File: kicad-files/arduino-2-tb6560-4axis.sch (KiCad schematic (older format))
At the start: 11 parts, among them J1 DB25_Female_MountingHoles, J2 Conn_01x03_Male, J3 Conn_01x02_Male, J4 Conn_01x02_Male, J5 Conn_01x03_Male, J6 Conn_01x02_Male, J7 Conn_01x03_Male, Q1 2N3904

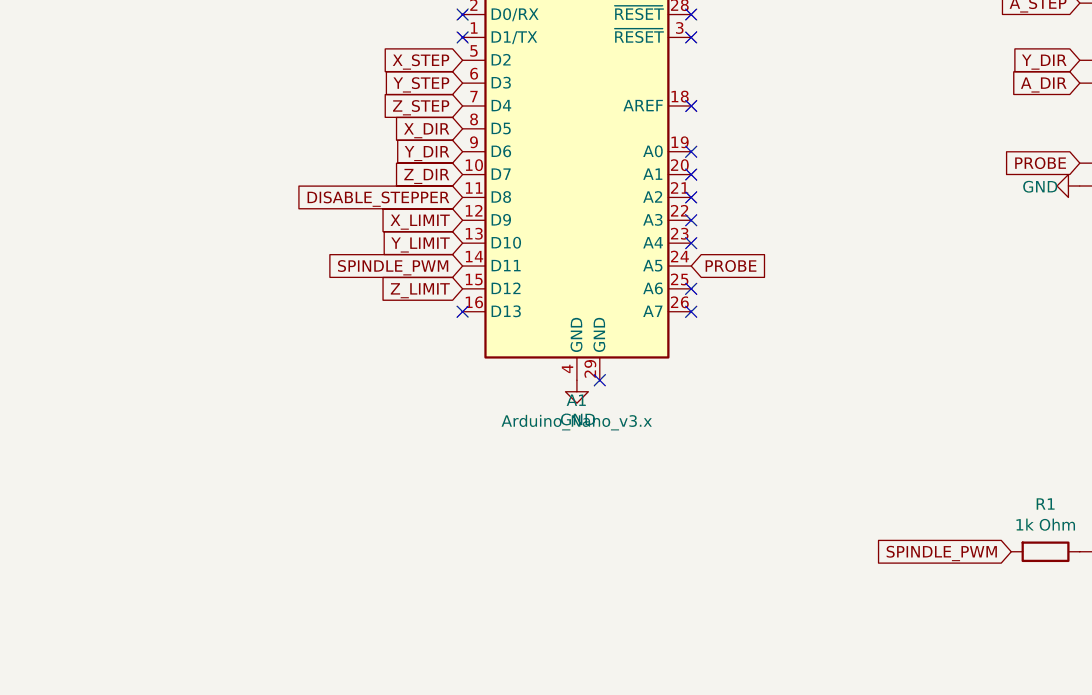
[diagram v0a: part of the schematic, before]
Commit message: added push buttons and jumper header for feed hold and cycle start/resume.
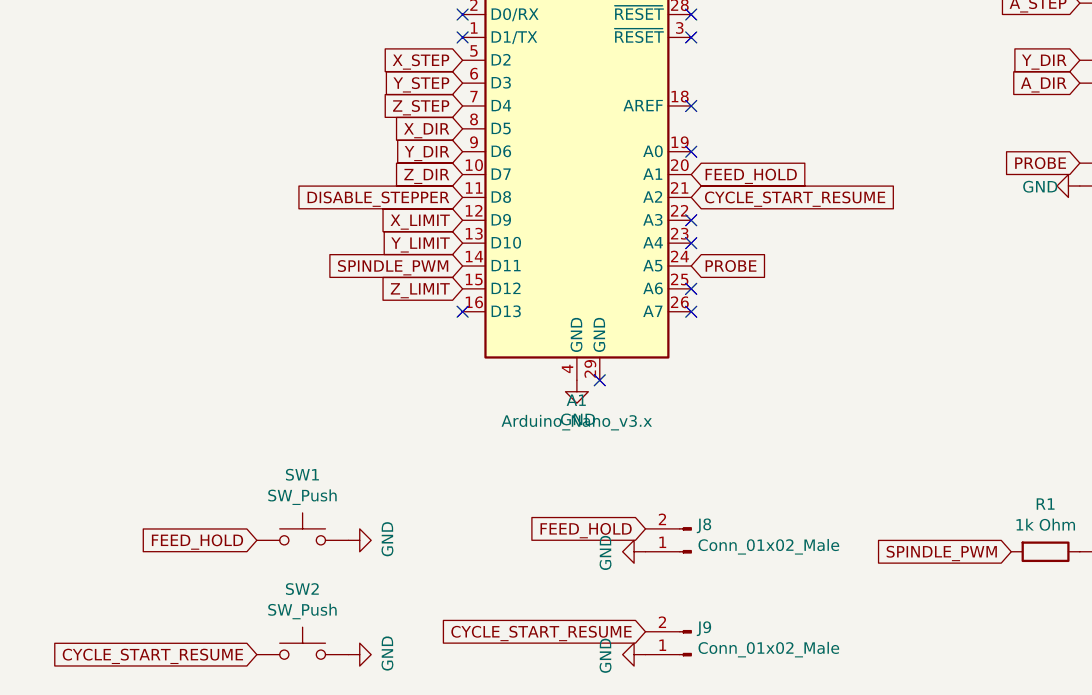
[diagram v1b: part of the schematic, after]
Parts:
- added J8, J9: Conn_01x02_Male, Connector_PinHeader_2.54mm:PinHeader_1x02_P2.54mm_Vertical, symbol Connector:Conn_01x02_Male
- added SW1, SW2: SW_Push, Button_Switch_THT:SW_PUSH_6mm_H7.3mm, symbol Switch:SW_Push
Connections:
- net GND: now also J8.1 (Pin_1), J9.1 (Pin_1), SW1.2, SW2.2
- net FEED_HOLD: now reaches A1.20 (A1)
- net FEED_HOLD: now also J8.2 (Pin_2), SW1.1
- net CYCLE_START_RESUME: now reaches A1.21 (A2)
- net CYCLE_START_RESUME: now also J9.2 (Pin_2), SW2.1
- no-connect marks 19 -> 17
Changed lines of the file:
@@
 NoConn ~ 4200 3850
 NoConn ~ 4200 3750
-NoConn ~ 4200 3650
-NoConn ~ 4200 3550
 NoConn ~ 4200 3450
 NoConn ~ 4200 3250
@@
 Text GLabel 5900 1500 0    50   Input ~ 0
 SPINDLE_PWM_SELECT
+$Comp
+L Switch:SW_Push SW1
+U 1 1 5F5A9D82
+P 2500 5150
+F 0 "SW1" H 2500 5435 50  0000 C CNN
+F 1 "SW_Push" H 2500 5344 50  0000 C CNN
+F 2 "Button_Switch_THT:SW_PUSH_6mm_H7.3mm" H 2500 5350 50  0001 C CNN
+F 3 "~" H 2500 5350 50  0001 C CNN
+	1    2500 5150
+	1    0    0    -1
+$EndComp
+Text GLabel 4200 3550 2    50   Input ~ 0
+FEED_HOLD
+Text GLabel 4200 3650 2    50   Input ~ 0
+CYCLE_START_RESUME
+$Comp
+L Switch:SW_Push SW2
+U 1 1 5F5AC1C4
+P 2500 5650
+F 0 "SW2" H 2500 5935 50  0000 C CNN
+F 1 "SW_Push" H 2500 5844 50  0000 C CNN
+F 2 "Button_Switch_THT:SW_PUSH_6mm_H7.3mm" H 2500 5850 50  0001 C CNN
+F 3 "~" H 2500 5850 50  0001 C CNN
+	1    2500 5650
+	1    0    0    -1
+$EndComp
+$Comp
+L power:GND #PWR0103
+U 1 1 5F5AC85F
+P 2700 5650
+F 0 "#PWR0103" H 2700 5400 50  0001 C CNN
+F 1 "GND" H 2705 5477 50  0000 C CNN
+F 2 "" H 2700 5650 50  0001 C CNN
+F 3 "" H 2700 5650 50  0001 C CNN
+	1    2700 5650
+	0    -1   -1   0
+$EndComp
+$Comp
+L power:GND #PWR0104
+U 1 1 5F5ACD90
+P 2700 5150
+F 0 "#PWR0104" H 2700 4900 50  0001 C CNN
+F 1 "GND" H 2705 4977 50  0000 C CNN
+F 2 "" H 2700 5150 50  0001 C CNN
+F 3 "" H 2700 5150 50  0001 C CNN
+	1    2700 5150
+	0    -1   -1   0
+$EndComp
+Text GLabel 2300 5150 0    50   Input ~ 0
+FEED_HOLD
+Text GLabel 2300 5650 0    50   Input ~ 0
+CYCLE_START_RESUME
+$Comp
+L Connector:Conn_01x02_Male J8
+U 1 1 5F5BC0DA
+P 4200 5200
+F 0 "J8" H 4172 5082 50  0000 R CNN
+F 1 "Conn_01x02_Male" H 4172 5173 50  0000 R CNN
+F 2 "Connector_PinHeader_2.54mm:PinHeader_1x02_P2.54mm_Vertical" H 4200 5200 50  0001 C CNN
+F 3 "~" H 4200 5200 50  0001 C CNN
+	1    4200 5200
+	-1   0    0    1
+$EndComp
+$Comp
+L Connector:Conn_01x02_Male J9
+U 1 1 5F5BC816
+P 4200 5650
+F 0 "J9" H 4172 5532 50  0000 R CNN
+F 1 "Conn_01x02_Male" H 4172 5623 50  0000 R CNN
+F 2 "Connector_PinHeader_2.54mm:PinHeader_1x02_P2.54mm_Vertical" H 4200 5650 50  0001 C CNN
+F 3 "~" H 4200 5650 50  0001 C CNN
+	1    4200 5650
+	-1   0    0    1
+$EndComp
+$Comp
+L power:GND #PWR0105
+U 1 1 5F5BCC4F
+P 4000 5200
+F 0 "#PWR0105" H 4000 4950 50  0001 C CNN
+F 1 "GND" H 4005 5027 50  0000 C CNN
+F 2 "" H 4000 5200 50  0001 C CNN
+F 3 "" H 4000 5200 50  0001 C CNN
+	1    4000 5200
+	0    1    1    0
+$EndComp
+$Comp
+L power:GND #PWR0106
+U 1 1 5F5BD17C
+P 4000 5650
+F 0 "#PWR0106" H 4000 5400 50  0001 C CNN
+F 1 "GND" H 4005 5477 50  0000 C CNN
+F 2 "" H 4000 5650 50  0001 C CNN
+F 3 "" H 4000 5650 50  0001 C CNN
+	1    4000 5650
+	0    1    1    0
+$EndComp
+Text GLabel 4000 5100 0    50   Input ~ 0
+FEED_HOLD
+Text GLabel 4000 5550 0    50   Input ~ 0
+CYCLE_START_RESUME
 $EndSCHEMATC

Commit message: more ideas for rev 1.3
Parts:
- added D1, D2, D3: LED, LED_THT:LED_D5.0mm, symbol Device:LED
- added R3, R4, R5: 1k Ohm, Resistor_THT:R_Axial_DIN0204_L3.6mm_D1.6mm_P5.08mm_Horizontal, symbol Device:R
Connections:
- net GND: now also D1.2 (A), D2.2 (A), D3.2 (A)
- net X_STEP: now also R3.2
- net Y_STEP: now also R4.2
- net Z_STEP: now also R5.2
- new net: D1.1 (K), R3.1
- new net: D2.1 (K), R4.1
- new net: D3.1 (K), R5.1
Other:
- moved on the sheet: Q1, R1, R2
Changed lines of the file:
@@
 L Device:R R1
 U 1 1 5F56F856
-P 5750 5200
-F 0 "R1" V 5543 5200 50  0000 C CNN
-F 1 "1k Ohm" V 5634 5200 50  0000 C CNN
-F 2 "Resistor_THT:R_Axial_DIN0204_L3.6mm_D1.6mm_P5.08mm_Horizontal" V 5680 5200 50  0001 C CNN
-F 3 "~" H 5750 5200 50  0001 C CNN
-	1    5750 5200
+P 6850 5600
+F 0 "R1" V 6643 5600 50  0000 C CNN
+F 1 "1k Ohm" V 6734 5600 50  0000 C CNN
+F 2 "Resistor_THT:R_Axial_DIN0204_L3.6mm_D1.6mm_P5.08mm_Horizontal" V 6780 5600 50  0001 C CNN
+F 3 "~" H 6850 5600 50  0001 C CNN
+	1    6850 5600
 	0    1    1    0
 $EndComp
@@
 L Device:R R2
 U 1 1 5F57191E
-P 6200 4450
-F 0 "R2" H 6270 4496 50  0000 L CNN
-F 1 "1K Ohm" H 6270 4405 50  0000 L CNN
-F 2 "Resistor_THT:R_Axial_DIN0204_L3.6mm_D1.6mm_P5.08mm_Horizontal" V 6130 4450 50  0001 C CNN
-F 3 "~" H 6200 4450 50  0001 C CNN
-	1    6200 4450
+P 7300 4850
+F 0 "R2" H 7370 4896 50  0000 L CNN
+F 1 "1K Ohm" H 7370 4805 50  0000 L CNN
+F 2 "Resistor_THT:R_Axial_DIN0204_L3.6mm_D1.6mm_P5.08mm_Horizontal" V 7230 4850 50  0001 C CNN
+F 3 "~" H 7300 4850 50  0001 C CNN
+	1    7300 4850
 	1    0    0    -1
 $EndComp
@@
 L Transistor_BJT:2N3904 Q1
 U 1 1 5F5721BB
-P 6100 5200
-F 0 "Q1" H 6290 5246 50  0000 L CNN
-F 1 "2N3904" H 6290 5155 50  0000 L CNN
-F 2 "Package_TO_SOT_THT:TO-92_Inline" H 6300 5125 50  0001 L CIN
-F 3 "https://www.fairchildsemi.com/datasheets/2N/2N3904.pdf" H 6100 5200 50  0001 L CNN
-	1    6100 5200
+P 7200 5600
+F 0 "Q1" H 7390 5646 50  0000 L CNN
+F 1 "2N3904" H 7390 5555 50  0000 L CNN
+F 2 "Package_TO_SOT_THT:TO-92_Inline" H 7400 5525 50  0001 L CIN
+F 3 "https://www.fairchildsemi.com/datasheets/2N/2N3904.pdf" H 7200 5600 50  0001 L CNN
+	1    7200 5600
 	1    0    0    -1
 $EndComp
 Text GLabel 3900 2450 1    50   Input ~ 0
 VCC
-Text GLabel 6200 4300 1    50   Input ~ 0
+Text GLabel 7300 4700 1    50   Input ~ 0
 VCC
-Text GLabel 5600 5200 0    50   Input ~ 0
+Text GLabel 6700 5600 0    50   Input ~ 0
 SPINDLE_PWM
 $Comp
 L power:GND #PWR0101
 U 1 1 5F581B0A
-P 6200 5400
-F 0 "#PWR0101" H 6200 5150 50  0001 C CNN
-F 1 "GND" H 6205 5227 50  0000 C CNN
-F 2 "" H 6200 5400 50  0001 C CNN
-F 3 "" H 6200 5400 50  0001 C CNN
-	1    6200 5400
+P 7300 5800
+F 0 "#PWR0101" H 7300 5550 50  0001 C CNN
+F 1 "GND" H 7305 5627 50  0000 C CNN
+F 2 "" H 7300 5800 50  0001 C CNN
+F 3 "" H 7300 5800 50  0001 C CNN
+	1    7300 5800
 	1    0    0    -1
 $EndComp
 Wire Wire Line
-	6200 5000 6200 4600
-Text GLabel 6200 4800 2    50   Input ~ 0
+	7300 5400 7300 5000
+Text GLabel 7300 5200 2    50   Input ~ 0
 SPINDLE_PWM_INVERTED
 Text GLabel 4200 3950 2    50   Input ~ 0
@@
 Text GLabel 4000 5550 0    50   Input ~ 0
 CYCLE_START_RESUME
+$Comp
+L Device:R R3
+U 1 1 5F5D16E5
+P 5900 4350
+F 0 "R3" V 5693 4350 50  0000 C CNN
+F 1 "1k Ohm" V 5784 4350 50  0000 C CNN
+F 2 "Resistor_THT:R_Axial_DIN0204_L3.6mm_D1.6mm_P5.08mm_Horizontal" V 5830 4350 50  0001 C CNN
+F 3 "~" H 5900 4350 50  0001 C CNN
+	1    5900 4350
+	0    1    1    0
+$EndComp
+$Comp
+L Device:R R4
+U 1 1 5F5D1BCB
+P 5900 4600
+F 0 "R4" V 5693 4600 50  0000 C CNN
+F 1 "1k Ohm" V 5784 4600 50  0000 C CNN
+F 2 "Resistor_THT:R_Axial_DIN0204_L3.6mm_D1.6mm_P5.08mm_Horizontal" V 5830 4600 50  0001 C CNN
+F 3 "~" H 5900 4600 50  0001 C CNN
+	1    5900 4600
+	0    1    1    0
+$EndComp
+$Comp
+L Device:R R5
+U 1 1 5F5D1F89
+P 5900 4850
+F 0 "R5" V 5693 4850 50  0000 C CNN
+F 1 "1k Ohm" V 5784 4850 50  0000 C CNN
+F 2 "Resistor_THT:R_Axial_DIN0204_L3.6mm_D1.6mm_P5.08mm_Horizontal" V 5830 4850 50  0001 C CNN
+F 3 "~" H 5900 4850 50  0001 C CNN
+	1    5900 4850
+	0    1    1    0
+$EndComp
+Text GLabel 5750 4350 0    50   Input ~ 0
+X_STEP
+Text GLabel 5750 4600 0    50   Input ~ 0
+Y_STEP
+Text GLabel 5750 4850 0    50   Input ~ 0
+Z_STEP
+$Comp
+L Device:LED D1
+U 1 1 5F5D402B
+P 6200 4350
+F 0 "D1" H 6193 4567 50  0000 C CNN
+F 1 "LED" H 6193 4476 50  0000 C CNN
+F 2 "LED_THT:LED_D5.0mm" H 6200 4350 50  0001 C CNN
+F 3 "~" H 6200 4350 50  0001 C CNN
+	1    6200 4350
+	1    0    0    -1
+$EndComp
+$Comp
+L Device:LED D2
+U 1 1 5F5D6475
+P 6200 4600
+F 0 "D2" H 6193 4817 50  0000 C CNN
+F 1 "LED" H 6193 4726 50  0000 C CNN
+F 2 "LED_THT:LED_D5.0mm" H 6200 4600 50  0001 C CNN
+F 3 "~" H 6200 4600 50  0001 C CNN
+	1    6200 4600
+	1    0    0    -1
+$EndComp
+$Comp
+L Device:LED D3
+U 1 1 5F5D6793
+P 6200 4850
+F 0 "D3" H 6193 5067 50  0000 C CNN
+F 1 "LED" H 6193 4976 50  0000 C CNN
+F 2 "LED_THT:LED_D5.0mm" H 6200 4850 50  0001 C CNN
+F 3 "~" H 6200 4850 50  0001 C CNN
+	1    6200 4850
+	1    0    0    -1
+$EndComp
+$Comp
+L power:GND #PWR0107
+U 1 1 5F5D732B
+P 6350 4350
+F 0 "#PWR0107" H 6350 4100 50  0001 C CNN
+F 1 "GND" H 6355 4177 50  0000 C CNN
+F 2 "" H 6350 4350 50  0001 C CNN
+F 3 "" H 6350 4350 50  0001 C CNN
+	1    6350 4350
+	0    -1   -1   0
+$EndComp
+$Comp
+L power:GND #PWR0108
+U 1 1 5F5D79DB
+P 6350 4600
+F 0 "#PWR0108" H 6350 4350 50  0001 C CNN
+F 1 "GND" H 6355 4427 50  0000 C CNN
+F 2 "" H 6350 4600 50  0001 C CNN
+F 3 "" H 6350 4600 50  0001 C CNN
+	1    6350 4600
+	0    -1   -1   0
+$EndComp
+$Comp
+L power:GND #PWR0109
+U 1 1 5F5D7D83
+P 6350 4850
+F 0 "#PWR0109" H 6350 4600 50  0001 C CNN
+F 1 "GND" H 6355 4677 50  0000 C CNN
+F 2 "" H 6350 4850 50  0001 C CNN
+F 3 "" H 6350 4850 50  0001 C CNN
+	1    6350 4850
+	0    -1   -1   0
+$EndComp
 $EndSCHEMATC

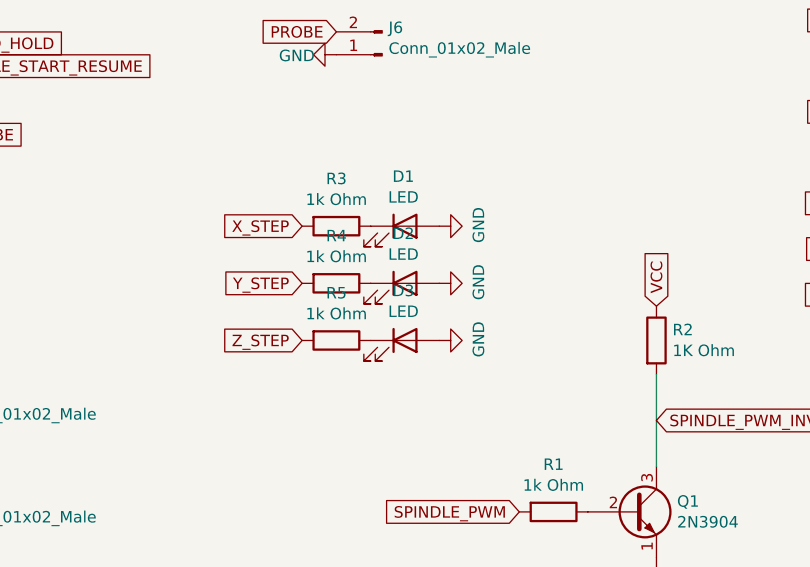
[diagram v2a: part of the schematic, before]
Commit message: rev. 1.4. fix wrong led orientation. fix wrong resistor footprint. reroute affected tracks.
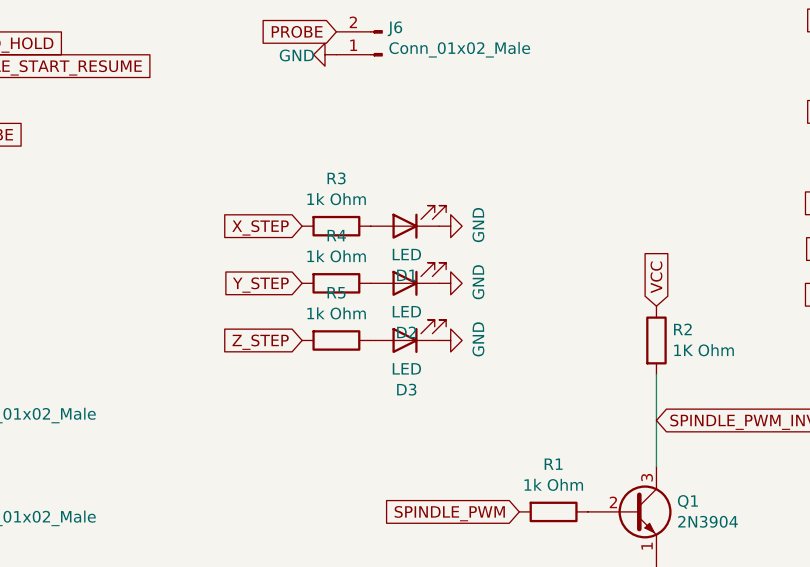
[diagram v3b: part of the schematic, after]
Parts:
- R1, R2, R3, R4, R5: footprint Resistor_THT:R_Axial_DIN0204_L3.6mm_D1.6mm_P5.08mm_Horizontal -> Resistor_THT:R_Axial_DIN0207_L6.3mm_D2.5mm_P7.62mm_Horizontal
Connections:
- net GND: now also D1.1 (K), D2.1 (K), D3.1 (K); no longer D1.2 (A), D2.2 (A), D3.2 (A)
- net at R3.1: now also D1.2 (A); no longer D1.1 (K)
- net at R4.1: now also D2.2 (A); no longer D2.1 (K)
- net at R5.1: now also D3.2 (A); no longer D3.1 (K)
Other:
- moved on the sheet: D1, D2, D3
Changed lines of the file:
@@
 F 0 "R1" V 6643 5600 50  0000 C CNN
 F 1 "1k Ohm" V 6734 5600 50  0000 C CNN
-F 2 "Resistor_THT:R_Axial_DIN0204_L3.6mm_D1.6mm_P5.08mm_Horizontal" V 6780 5600 50  0001 C CNN
+F 2 "Resistor_THT:R_Axial_DIN0207_L6.3mm_D2.5mm_P7.62mm_Horizontal" V 6780 5600 50  0001 C CNN
 F 3 "~" H 6850 5600 50  0001 C CNN
 	1    6850 5600
@@
 F 0 "R2" H 7370 4896 50  0000 L CNN
 F 1 "1K Ohm" H 7370 4805 50  0000 L CNN
-F 2 "Resistor_THT:R_Axial_DIN0204_L3.6mm_D1.6mm_P5.08mm_Horizontal" V 7230 4850 50  0001 C CNN
+F 2 "Resistor_THT:R_Axial_DIN0207_L6.3mm_D2.5mm_P7.62mm_Horizontal" V 7230 4850 50  0001 C CNN
 F 3 "~" H 7300 4850 50  0001 C CNN
 	1    7300 4850
@@
 F 0 "R3" V 5693 4350 50  0000 C CNN
 F 1 "1k Ohm" V 5784 4350 50  0000 C CNN
-F 2 "Resistor_THT:R_Axial_DIN0204_L3.6mm_D1.6mm_P5.08mm_Horizontal" V 5830 4350 50  0001 C CNN
+F 2 "Resistor_THT:R_Axial_DIN0207_L6.3mm_D2.5mm_P7.62mm_Horizontal" V 5830 4350 50  0001 C CNN
 F 3 "~" H 5900 4350 50  0001 C CNN
 	1    5900 4350
@@
 F 0 "R4" V 5693 4600 50  0000 C CNN
 F 1 "1k Ohm" V 5784 4600 50  0000 C CNN
-F 2 "Resistor_THT:R_Axial_DIN0204_L3.6mm_D1.6mm_P5.08mm_Horizontal" V 5830 4600 50  0001 C CNN
+F 2 "Resistor_THT:R_Axial_DIN0207_L6.3mm_D2.5mm_P7.62mm_Horizontal" V 5830 4600 50  0001 C CNN
 F 3 "~" H 5900 4600 50  0001 C CNN
 	1    5900 4600
@@
 F 0 "R5" V 5693 4850 50  0000 C CNN
 F 1 "1k Ohm" V 5784 4850 50  0000 C CNN
-F 2 "Resistor_THT:R_Axial_DIN0204_L3.6mm_D1.6mm_P5.08mm_Horizontal" V 5830 4850 50  0001 C CNN
+F 2 "Resistor_THT:R_Axial_DIN0207_L6.3mm_D2.5mm_P7.62mm_Horizontal" V 5830 4850 50  0001 C CNN
 F 3 "~" H 5900 4850 50  0001 C CNN
 	1    5900 4850
@@
 F 3 "~" H 6200 4350 50  0001 C CNN
 	1    6200 4350
-	1    0    0    -1
+	-1   0    0    1
+$EndComp
+$Comp
+L Device:LED D3
+U 1 1 5F5D6793
+P 6200 4850
+F 0 "D3" H 6193 5067 50  0000 C CNN
+F 1 "LED" H 6193 4976 50  0000 C CNN
+F 2 "LED_THT:LED_D5.0mm" H 6200 4850 50  0001 C CNN
+F 3 "~" H 6200 4850 50  0001 C CNN
+	1    6200 4850
+	-1   0    0    1
+$EndComp
+$Comp
+L power:GND #PWR0107
+U 1 1 5F5D732B
+P 6350 4350
+F 0 "#PWR0107" H 6350 4100 50  0001 C CNN
+F 1 "GND" H 6355 4177 50  0000 C CNN
+F 2 "" H 6350 4350 50  0001 C CNN
+F 3 "" H 6350 4350 50  0001 C CNN
+	1    6350 4350
+	0    -1   -1   0
+$EndComp
+$Comp
+L power:GND #PWR0108
+U 1 1 5F5D79DB
+P 6350 4600
+F 0 "#PWR0108" H 6350 4350 50  0001 C CNN
+F 1 "GND" H 6355 4427 50  0000 C CNN
+F 2 "" H 6350 4600 50  0001 C CNN
+F 3 "" H 6350 4600 50  0001 C CNN
+	1    6350 4600
+	0    -1   -1   0
+$EndComp
+$Comp
+L power:GND #PWR0109
+U 1 1 5F5D7D83
+P 6350 4850
+F 0 "#PWR0109" H 6350 4600 50  0001 C CNN
+F 1 "GND" H 6355 4677 50  0000 C CNN
+F 2 "" H 6350 4850 50  0001 C CNN
+F 3 "" H 6350 4850 50  0001 C CNN
+	1    6350 4850
+	0    -1   -1   0
 $EndComp
 $Comp
@@
 F 3 "~" H 6200 4600 50  0001 C CNN
 	1    6200 4600
-	1    0    0    -1
-$EndComp
-$Comp
-L Device:LED D3
-U 1 1 5F5D6793
-P 6200 4850
-F 0 "D3" H 6193 5067 50  0000 C CNN
-F 1 "LED" H 6193 4976 50  0000 C CNN
-F 2 "LED_THT:LED_D5.0mm" H 6200 4850 50  0001 C CNN
-F 3 "~" H 6200 4850 50  0001 C CNN
-	1    6200 4850
-	1    0    0    -1
-$EndComp
-$Comp
-L power:GND #PWR0107
-U 1 1 5F5D732B
-P 6350 4350
-F 0 "#PWR0107" H 6350 4100 50  0001 C CNN
-F 1 "GND" H 6355 4177 50  0000 C CNN
-F 2 "" H 6350 4350 50  0001 C CNN
-F 3 "" H 6350 4350 50  0001 C CNN
-	1    6350 4350
-	0    -1   -1   0
-$EndComp
-$Comp
-L power:GND #PWR0108
-U 1 1 5F5D79DB
-P 6350 4600
-F 0 "#PWR0108" H 6350 4350 50  0001 C CNN
-F 1 "GND" H 6355 4427 50  0000 C CNN
-F 2 "" H 6350 4600 50  0001 C CNN
-F 3 "" H 6350 4600 50  0001 C CNN
-	1    6350 4600
-	0    -1   -1   0
-$EndComp
-$Comp
-L power:GND #PWR0109
-U 1 1 5F5D7D83
-P 6350 4850
-F 0 "#PWR0109" H 6350 4600 50  0001 C CNN
-F 1 "GND" H 6355 4677 50  0000 C CNN
-F 2 "" H 6350 4850 50  0001 C CNN
-F 3 "" H 6350 4850 50  0001 C CNN
-	1    6350 4850
-	0    -1   -1   0
+	-1   0    0    1
 $EndComp
 $EndSCHEMATC
